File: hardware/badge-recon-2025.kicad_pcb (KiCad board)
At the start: 2 copper layers, 78.1 x 100 mm, 72 parts, among them J3 Battery, J5 OLED, P1 USB_C_Plug_USB2.0, Q1 DMG3415U-7, SW1 SW_Push, SW2 SW_Push, SW3 ON, SW4 SOURCE MAG, SW5 SW_Push, SW6 SW_Push, SW7 RESET, U1 PN7150B0HN_C11002E-PN7150B0HN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, U2 RP2040, U4 AP2112K-3.3, U6 W25Q16JV, U7 TC4424, Y1 27.12Mhz, Y2 12Mhz

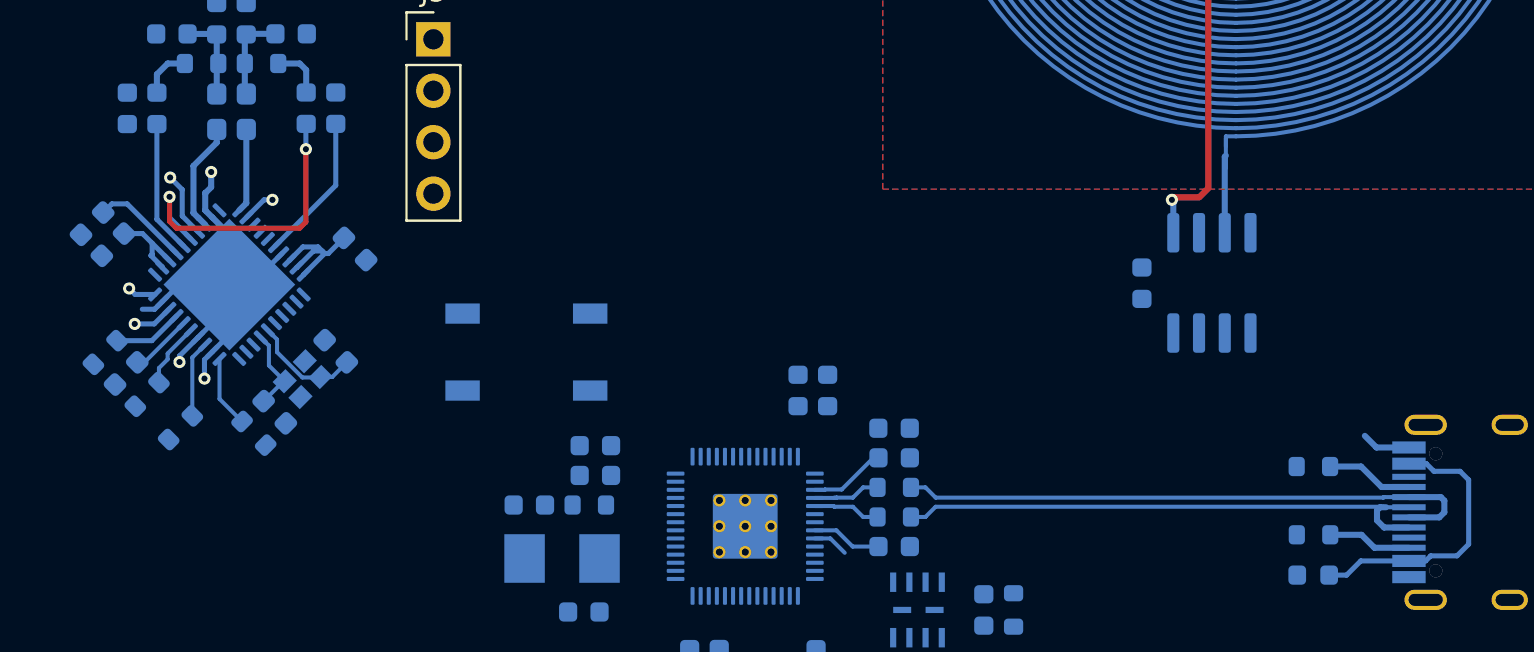
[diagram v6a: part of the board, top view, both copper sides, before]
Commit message: feat(Hw): update part numbers for JLCPCB assembly
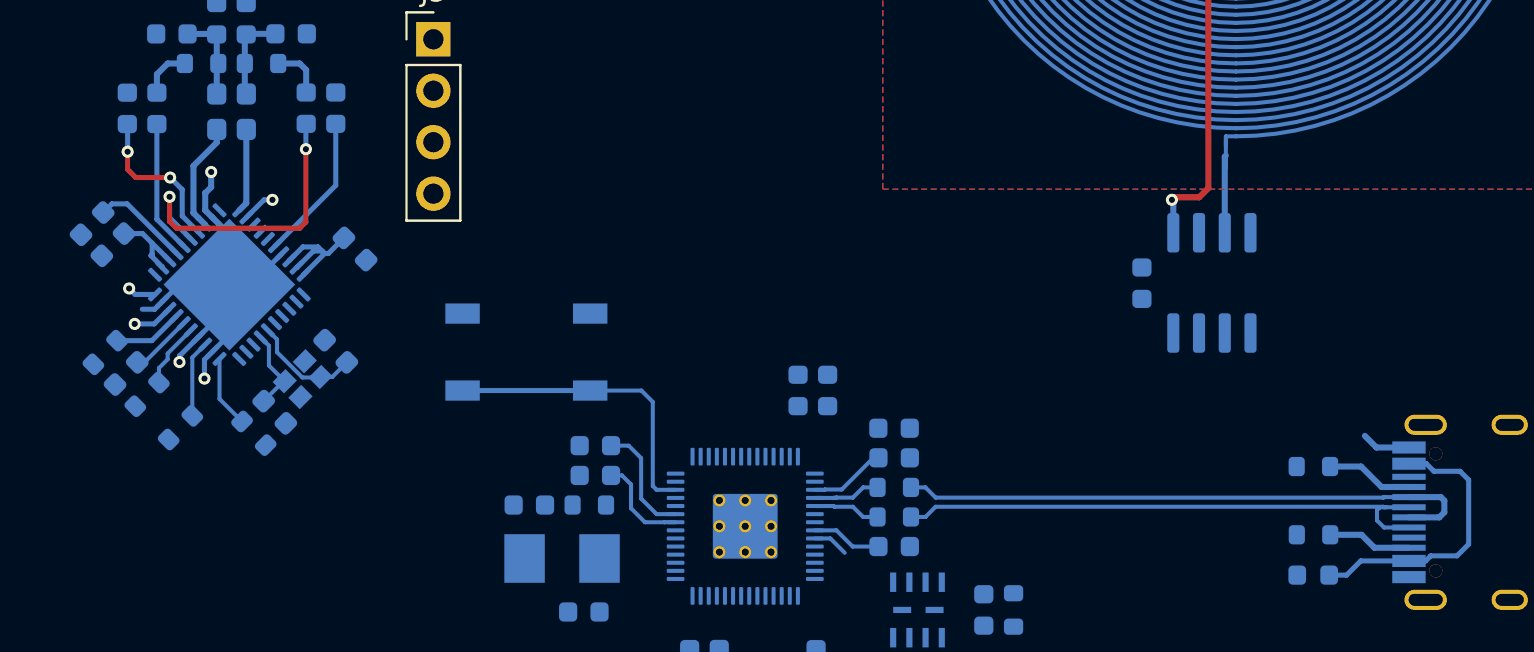
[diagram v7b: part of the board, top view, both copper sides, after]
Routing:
- net /RST: track 0.00 -> 15.0 mm
- net +1V2: track 7.27 -> 13.0 mm
- net +3V3: track 14.6 -> 19.5 mm
- net Net-(U1-VDD(MID)): track 3.25 -> 7.76 mm, vias 1 -> 2
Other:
- board text added: "- Check PN7150 crystal - Check RP2040 crystal"
- board text removed: "- Check PN7150 crystal - Change flash memmory packaging - Check switch avaaiability - Check RP2040 crystal - Check fuse"
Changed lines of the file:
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@@
 		(layer "Edge.Cuts")
 	)
-	(gr_text "- Check PN7150 crystal\n- Change flash memmory packaging \n- Check switch avaaiability\n- Check RP2040 crystal\n- Check fuse "
+	(gr_text "- Check PN7150 crystal\n- Check RP2040 crystal"
 		(at 196.825 72.975 0)
 		(layer "User.1")
@@
 	)
 	(segment
+		(start 145.575 95.075)
+		(end 145.13 94.63)
+		(width 0.2)
+		(layer "B.Cu")
+		(net 7)
+	)
+	(segment
+		(start 145.13 94.63)
+		(end 144.59029 94.63)
+		(width 0.2)
+		(layer "B.Cu")
+		(net 7)
+	)
+	(segment
+		(start 146.266 96.941)
+		(end 145.575 96.25)
+		(width 0.2)
+		(layer "B.Cu")
+		(net 7)
+	)
+	(segment
 		(start 128.001903 83.309651)
 		(end 131 80.311554)
@@
 	)
 	(segment
+		(start 145.575 96.25)
+		(end 145.575 95.075)
+		(width 0.2)
+		(layer "B.Cu")
+		(net 7)
+	)
+	(segment
 		(start 122.433436 84.333436)
 		(end 121.875 83.775)
@@
 	)
 	(segment
+		(start 147.239726 96.94)
+		(end 147.238726 96.941)
+		(width 0.2)
+		(layer "B.Cu")
+		(net 7)
+	)
+	(segment
 		(start 121.460233 82.69)
 		(end 121.935117 83.164883)
@@
 	)
 	(segment
+		(start 147.775 96.94)
+		(end 147.239726 96.94)
+		(width 0.2)
+		(layer "B.Cu")
+		(net 7)
+	)
+	(segment
+		(start 147.238726 96.941)
+		(end 146.266 96.941)
+		(width 0.2)
+		(layer "B.Cu")
+		(net 7)
+	)
+	(segment
 		(start 122.433436 84.37031)
 		(end 122.433436 84.333436)
@@
 		(layer "B.Cu")
 		(net 7)
+	)
+	(segment
+		(start 120.725 79.525)
+		(end 120.725 78.65)
+		(width 0.25)
+		(layer "F.Cu")
+		(net 8)
+	)
+	(segment
+		(start 121.125 79.925)
+		(end 120.825 79.625)
+		(width 0.25)
+		(layer "F.Cu")
+		(net 8)
+	)
+	(segment
+		(start 122.825 79.925)
+		(end 121.125 79.925)
+		(width 0.25)
+		(layer "F.Cu")
+		(net 8)
+	)
+	(segment
+		(start 120.825 79.625)
+		(end 120.725 79.525)
+		(width 0.25)
+		(layer "F.Cu")
+		(net 8)
 	)
 	(via
@@
 		(net 8)
 	)
+	(via
+		(at 120.725 78.65)
+		(size 0.6)
+		(drill 0.3)
+		(layers "F.Cu" "B.Cu")
+		(net 8)
+	)
+	(segment
+		(start 120.725 78.65)
+		(end 120.725 77.3)
+		(width 0.25)
+		(layer "B.Cu")
+		(net 8)
+	)
+	(segment
+		(start 120.725 77.3)
+		(end 120.71 77.285)
+		(width 0.25)
+		(layer "B.Cu")
+		(net 8)
+	)
 	(segment
 		(start 124.201205 82.602543)
@@
 	)
 	(segment
+		(start 146.075 95.775)
+		(end 146.075 93.775)
+		(width 0.2)
+		(layer "B.Cu")
+		(net 10)
+	)
+	(segment
+		(start 146.075 93.775)
+		(end 145.46 93.16)
+		(width 0.2)
+		(layer "B.Cu")
+		(net 10)
+	)
+	(segment
 		(start 155.135 95.34)
 		(end 155.151 95.324)
@@
 	)
 	(segment
+		(start 146.84 96.54)
+		(end 146.075 95.775)
+		(width 0.2)
+		(layer "B.Cu")
+		(net 10)
+	)
+	(segment
+		(start 145.46 93.16)
+		(end 144.59029 93.16)
+		(width 0.2)
+		(layer "B.Cu")
+		(net 10)
+	)
+	(segment
 		(start 157.54 93.76)
 		(end 157.79029 93.76)
@@
 		(start 157.79029 98.14)
 		(end 156.515 98.14)
+		(width 0.2)
+		(layer "B.Cu")
+		(net 10)
+	)
+	(segment
+		(start 147.775 96.54)
+		(end 146.84 96.54)
 		(width 0.2)
 		(layer "B.Cu")
@@
 		(start 182.55 96.2)
 		(end 182.85 96.2)
-		(width 0.3)
+		(width 0.2)
 		(layer "B.Cu")
 		(net 33)
@@
 		(start 182.4 96.35)
 		(end 182.55 96.2)
-		(width 0.3)
+		(width 0.2)
 		(layer "B.Cu")
 		(net 33)
@@
 		(start 183.9775 97.2)
 		(end 182.75 97.2)
-		(width 0.3)
+		(width 0.2)
 		(layer "B.Cu")
 		(net 33)
@@
 		(start 182.4 96.85)
 		(end 182.4 96.35)
-		(width 0.3)
+		(width 0.2)
 		(layer "B.Cu")
 		(net 33)
@@
 		(start 182.75 97.2)
 		(end 182.4 96.85)
-		(width 0.3)
+		(width 0.2)
 		(layer "B.Cu")
 		(net 33)
@@
 		(net 44)
 	)
+	(segment
+		(start 137.26 90.44)
+		(end 143.56 90.44)
+		(width 0.25)
+		(layer "B.Cu")
+		(net 45)
+	)
+	(segment
+		(start 146.84 95.34)
+		(end 146.65 95.15)
+		(width 0.2)
+		(layer "B.Cu")
+		(net 45)
+	)
+	(segment
+		(start 147.775 95.34)
+		(end 146.84 95.34)
+		(width 0.2)
+		(layer "B.Cu")
+		(net 45)
+	)
+	(segment
+		(start 146.09 90.44)
+		(end 143.56 90.44)
+		(width 0.2)
+		(layer "B.Cu")
+		(net 45)
+	)
+	(segment
+		(start 146.65 91)
+		(end 146.09 90.44)
+		(width 0.2)
+		(layer "B.Cu")
+		(net 45)
+	)
+	(segment
+		(start 146.65 95.15)
+		(end 146.65 91)
+		(width 0.2)
+		(layer "B.Cu")
+		(net 45)
+	)
 	(via

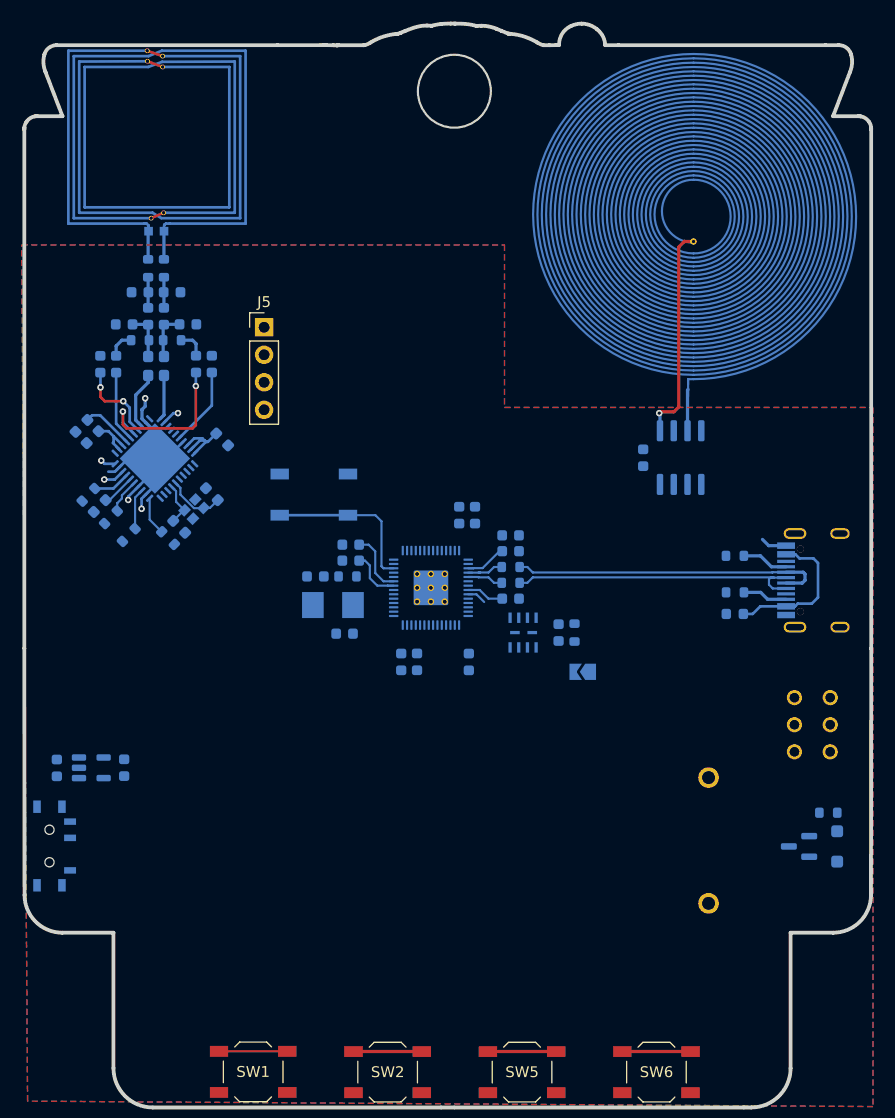
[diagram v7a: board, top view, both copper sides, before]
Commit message: feat(Hw): add expansor, 0 unconnected, missing pn7150 crystal
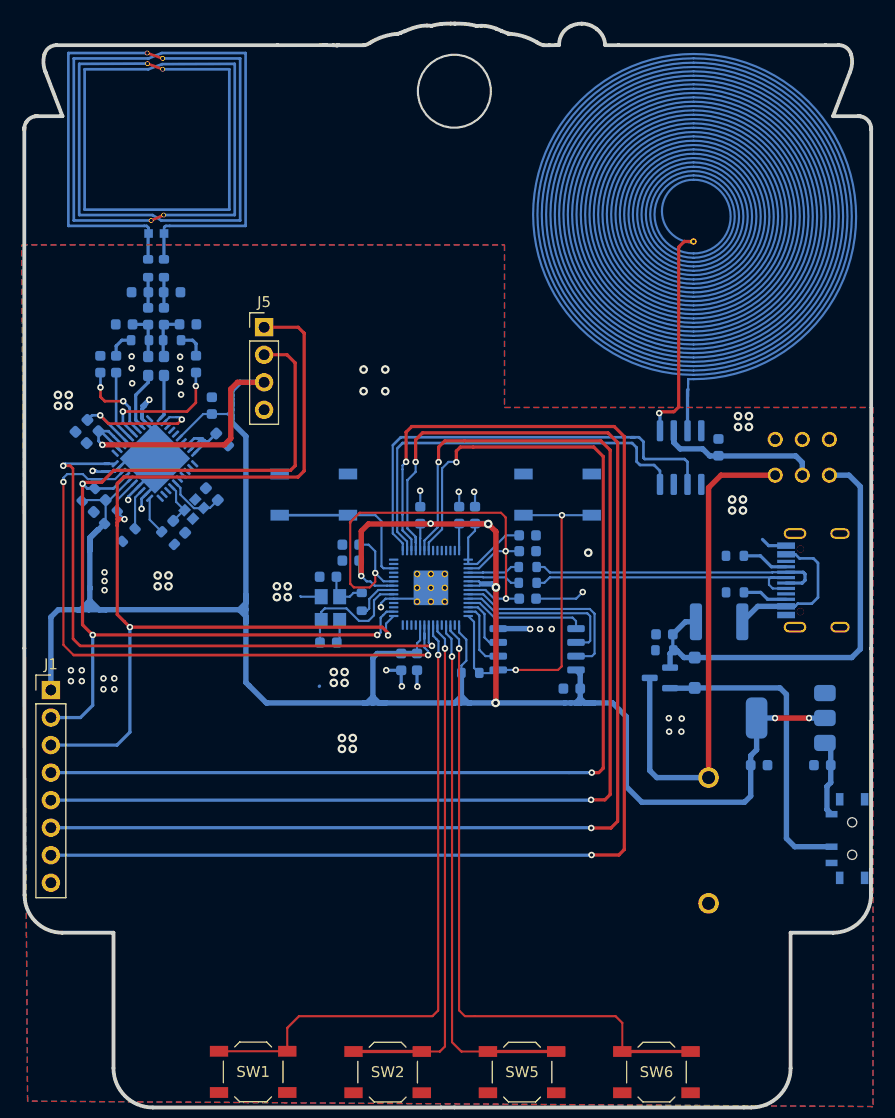
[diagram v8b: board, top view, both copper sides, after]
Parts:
- removed JP1: BOOT, Jumper:SolderJumper-2_P1.3mm_Open_TrianglePad1.0x1.5mm
- removed the U4 at (119.9, 113.7)
- added C32: 10uF, Capacitor_SMD:C_0603_1608Metric, B.Cu at (172.8, 101.4)
- added J1: EXPANSION, Connector_PinHeader_2.54mm:PinHeader_1x08_P2.54mm_Vertical, F.Cu at (116.2, 106.6)
- added SW8: BOOT, Button_Switch_SMD:SW_SPST_TL3342, B.Cu at (162.9, 88.5)
- added U3: AP2114H, Package_TO_SOT_SMD:SOT-223-3_TabPin2, B.Cu at (184.4, 109.2)
- added kibuzzard-6806AEF7: G***, kibuzzard-6806AEF7, B.Cu at (121.0, 106.6)
- added kibuzzard-6806AF29: G***, kibuzzard-6806AF29, B.Cu at (120.7, 111.7)
- added kibuzzard-6806AF2D: G***, kibuzzard-6806AF2D, B.Cu at (120.6, 109.2)
- added kibuzzard-6806AF43: G***, kibuzzard-6806AF43, B.Cu at (121.7, 114.2)
- added kibuzzard-6806AF6E: G***, kibuzzard-6806AF6E, B.Cu at (121.7, 116.8)
- added kibuzzard-6806AF7F: G***, kibuzzard-6806AF7F, B.Cu at (121.6, 119.3)
- added kibuzzard-6806AF94: G***, kibuzzard-6806AF94, B.Cu at (121.7, 121.8)
- added kibuzzard-6806AFC6: G***, kibuzzard-6806AFC6, B.Cu at (120.7, 124.4)
- added kibuzzard-6806B2E8: G***, kibuzzard-6806B2E8, B.Cu at (189.0, 89.0)
- added kibuzzard-6806B2F9: G***, kibuzzard-6806B2F9, B.Cu at (181.5, 88.9)
- C1, C2: value 27pF -> 15pF
- C25, C26: value 252.8pF -> 270pF
- C27, C28: value 63.3pF/50V -> 62pF/50V
- C30, C31: value 813.5pF -> 820pF
- F1: footprint Fuse:Fuse_0603_1608Metric -> Fuse:Fuse_1812_4532Metric
- R18, R19: value 0.39R -> 0.33R
- U4: renamed from U6; footprint Footprints:W25Q16JVUUIQ -> Package_SO:SOIC-8_5.3x5.3mm_P1.27mm
- Y2: value 12Mhz -> ABM8-272-T3; footprint Crystal:Crystal_SMD_5032-2Pin_5.0x3.2mm -> Crystal:Crystal_SMD_Abracon_ABM8G-4Pin_3.2x2.5mm
- moved SW3 74.1 mm to (190.1, 120.3), turned to -90 degrees
- moved C22 70.6 mm to (187.3, 113.5), turned to 180 degrees
- moved C29 58.6 mm to (181.5, 113.5), turned to 0 degrees
- moved SW4 24.7 mm to (185.5, 85.1), turned to 180 degrees
- moved R14 21.3 mm to (172.8, 102.9)
- moved D4 20.7 mm to (175.6, 105.0)
- moved Q1 20.2 mm to (172.3, 105.5)
- moved C19 14.3 mm to (150.2, 90.4), turned to 90 degrees
- moved R20 10.3 mm to (154.8, 105.0), turned to 0 degrees
- moved C34 7.01 mm to (177.7, 84.2), turned to 90 degrees
- moved C33 5.31 mm to (164.2, 106.4), turned to 180 degrees
- moved C6 3.83 mm to (131.0, 80.3)
- moved R3 2.68 mm to (144.8, 98.4), turned to -90 degrees
- moved U4 2.01 mm to (161.0, 102.8), turned to 0 degrees
- moved C1 1.71 mm to (141.8, 102.2), turned to 0 degrees
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- renumbered U7 to U5
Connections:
- C22 pad 1: Net-(SW3-B) -> Net-(SW3-A)
- SW3 pad 1: Net-(D4-K) -> Net-(SW3-A)
- SW3 pad 2: Net-(SW3-B) -> Net-(D4-K)
- U2 pad 29: /IN_B -> /IN_A
- U2 pad 3: unconnected-(U2-GPIO1-Pad3) -> /BUTTON_4
- U2 pad 30: /IN_A -> /IN_B
- U2 pad 31: /BUTTON_1 -> /GPIO20
- U2 pad 32: /BUTTON_2 -> /GPIO21
- U2 pad 34: /BUTTON_3 -> /GPIO22
- U2 pad 35: /BUTTON_4 -> /GPIO23
- U2 pad 4: unconnected-(U2-GPIO2-Pad4) -> /BUTTON_3
- U2 pad 6: unconnected-(U2-GPIO4-Pad6) -> /BUTTON_2
- U2 pad 7: unconnected-(U2-GPIO5-Pad7) -> /BUTTON_1
- Y2 pad 2: Net-(C2-Pad1) -> GND
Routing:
- net +3V3: track 19.5 -> 272.9 mm, vias 0 -> 8
- net /GPIO20: track 0.00 -> 123.4 mm, vias 0 -> 2
- net /GPIO21: track 0.00 -> 118.2 mm, vias 0 -> 2
- net /GPIO22: track 0.00 -> 110.1 mm, vias 0 -> 2
- net /GPIO23: track 0.00 -> 104.7 mm, vias 0 -> 2
- net /SDA: track 3.24 -> 99.4 mm, vias 0 -> 3
- net /SCL: track 3.44 -> 92.3 mm, vias 0 -> 3
- net /IRQ: track 2.02 -> 61.3 mm, vias 1 -> 2
- net /VEN: track 1.40 -> 57.4 mm, vias 1 -> 2
- net /BUTTON_4: track 6.30 -> 60.4 mm, vias 0 -> 1
- net /BUTTON_1: track 6.30 -> 58.8 mm, vias 0 -> 1
- net +BATT: track 0.00 -> 47.6 mm
- net /BUTTON_3: track 6.30 -> 48.7 mm, vias 0 -> 1
- net VBUS: track 0.00 -> 42.1 mm
- net /IN_A: track 0.00 -> 41.8 mm
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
